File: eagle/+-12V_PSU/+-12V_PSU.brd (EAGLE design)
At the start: 93.7 x 71.1 mm, 23 parts, among them CN1 OUT, IC1 7812T, IC2 7912

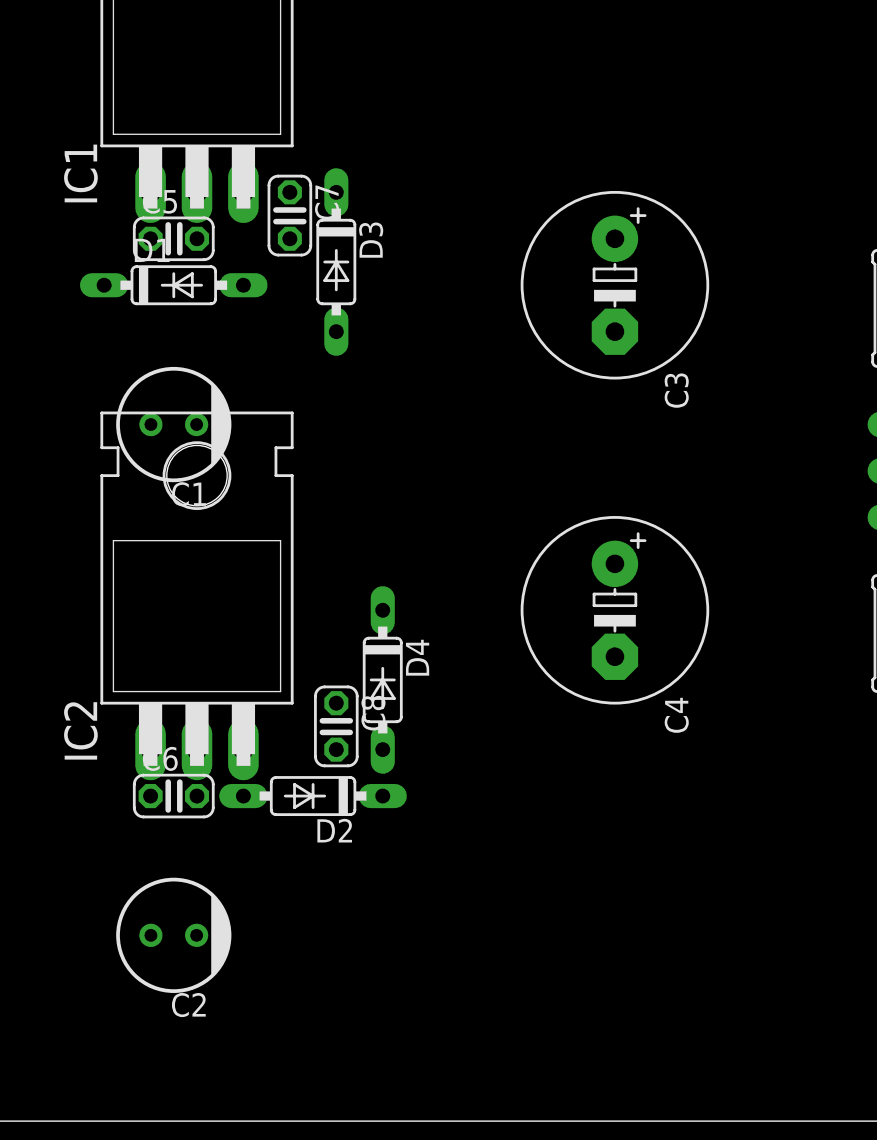
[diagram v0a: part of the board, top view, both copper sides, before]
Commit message: Add: +-12V_PSU eagle files
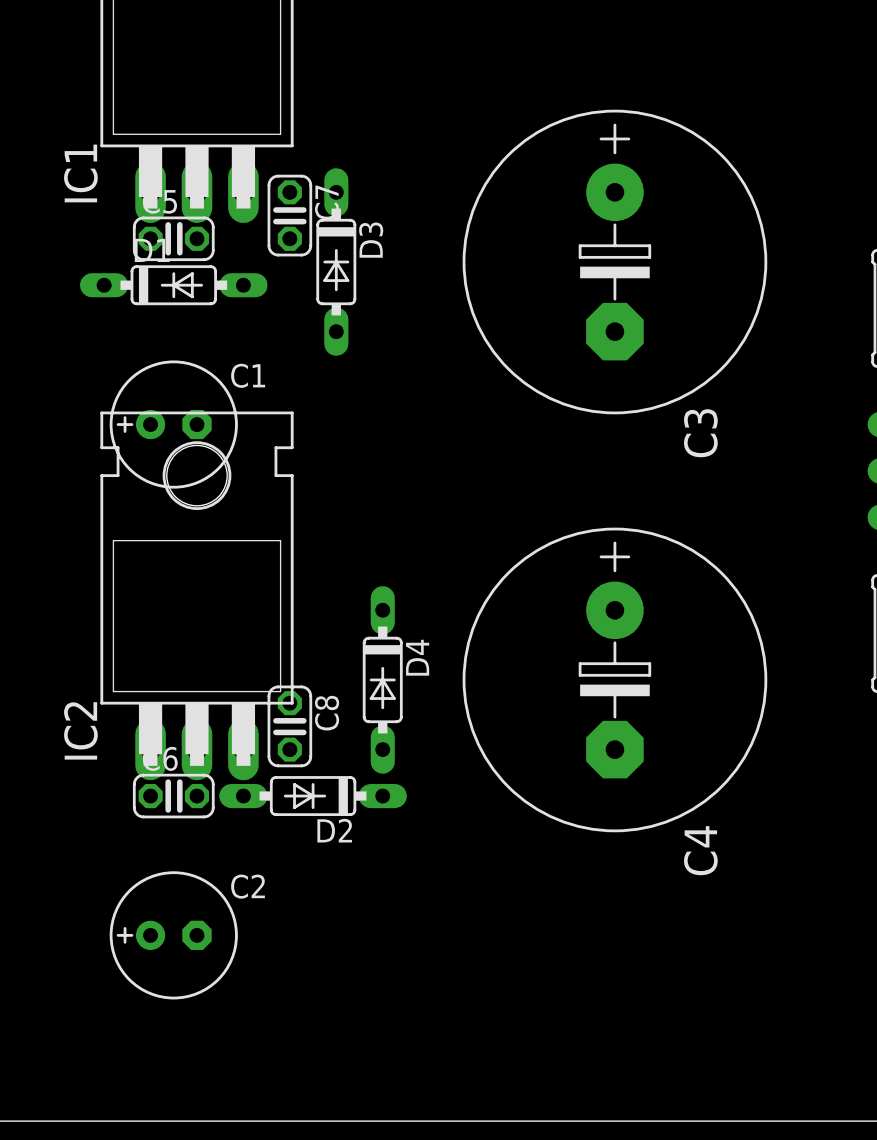
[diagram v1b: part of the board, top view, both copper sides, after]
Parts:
- C1, C2: device rcl:SANYO-OSCON_C6 -> rcl:E2,5-7
- C3, C4: device rcl:E5-10,5 -> rcl:E7,5-16
- moved C4 3.81 mm to (71.1, 24.1)
- moved C8 2.54 mm to (53.3, 21.6)
- moved C3 1.27 mm to (71.1, 47.0)
- turned C1 to 0 degrees
- turned C2 to 0 degrees
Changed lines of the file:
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@@
 <wire x1="2.54" y1="2.54" x2="2.54" y2="12.7" width="0" layer="100"/>
 <wire x1="2.54" y1="12.7" x2="2.54" y2="25.4" width="0" layer="100"/>
-<wire x1="2.54" y1="25.4" x2="2.54" y2="38.1" width="0" layer="100"/>
-<wire x1="2.54" y1="38.1" x2="2.54" y2="50.8" width="0" layer="100"/>
+<wire x1="2.54" y1="25.4" x2="5.08" y2="38.1" width="0" layer="100"/>
+<wire x1="5.08" y1="38.1" x2="2.54" y2="50.8" width="0" layer="100"/>
 <wire x1="2.54" y1="50.8" x2="2.54" y2="63.5" width="0" layer="100"/>
 <wire x1="2.54" y1="63.5" x2="2.54" y2="68.58" width="0" layer="100"/>
@@
 <wire x1="88.9" y1="2.54" x2="88.9" y2="68.58" width="0" layer="100"/>
 <wire x1="91.44" y1="2.54" x2="91.44" y2="12.7" width="0" layer="100"/>
-<wire x1="91.44" y1="12.7" x2="91.44" y2="38.1" width="0" layer="100"/>
-<wire x1="91.44" y1="38.1" x2="91.44" y2="50.8" width="0" layer="100"/>
+<wire x1="91.44" y1="12.7" x2="93.98" y2="38.1" width="0" layer="100"/>
+<wire x1="93.98" y1="38.1" x2="91.44" y2="50.8" width="0" layer="100"/>
 <wire x1="91.44" y1="50.8" x2="91.44" y2="68.58" width="0" layer="100"/>
 <wire x1="2.54" y1="12.7" x2="91.44" y2="12.7" width="0" layer="100"/>
 <wire x1="2.54" y1="25.4" x2="91.44" y2="25.4" width="0" layer="100"/>
-<wire x1="2.54" y1="38.1" x2="91.44" y2="38.1" width="0" layer="100"/>
+<wire x1="5.08" y1="38.1" x2="93.98" y2="38.1" width="0" layer="100"/>
 <wire x1="2.54" y1="63.5" x2="91.44" y2="63.5" width="0" layer="100"/>
 <wire x1="2.54" y1="68.58" x2="12.7" y2="68.58" width="0" layer="100"/>
@@
 </autorouter>
 <elements>
-<element name="C1" library="rcl" library_urn="urn:adsk.eagle:library:334" package="SANYO-OSCON_C6" package3d_urn="urn:adsk.eagle:package:23444/1" value="100uF" x="46.99" y="38.1" rot="R180">
-<attribute name="SPICEPREFIX" value="C" x="46.99" y="38.1" size="1.778" layer="27" rot="R180" display="off"/>
-</element>
-<element name="C2" library="rcl" library_urn="urn:adsk.eagle:library:334" package="SANYO-OSCON_C6" package3d_urn="urn:adsk.eagle:package:23444/1" value="100uF" x="46.99" y="10.16" rot="R180">
-<attribute name="SPICEPREFIX" value="C" x="46.99" y="10.16" size="1.778" layer="27" rot="R180" display="off"/>
-</element>
-<element name="C3" library="rcl" library_urn="urn:adsk.eagle:library:334" package="E5-10,5" package3d_urn="urn:adsk.eagle:package:23372/1" value="470uF" x="71.12" y="45.72" rot="R270">
-<attribute name="SPICEPREFIX" value="C" x="71.12" y="45.72" size="1.778" layer="27" rot="R270" display="off"/>
-</element>
-<element name="C4" library="rcl" library_urn="urn:adsk.eagle:library:334" package="E5-10,5" package3d_urn="urn:adsk.eagle:package:23372/1" value="470uF" x="71.12" y="27.94" rot="R270">
-<attribute name="SPICEPREFIX" value="C" x="71.12" y="27.94" size="1.778" layer="27" rot="R270" display="off"/>
+<element name="C1" library="rcl" library_urn="urn:adsk.eagle:library:334" package="E2,5-7" package3d_urn="urn:adsk.eagle:package:23345/1" value="100uF" x="46.99" y="38.1">
+<attribute name="SPICEPREFIX" value="C" x="46.99" y="38.1" size="1.778" layer="27" display="off"/>
+</element>
+<element name="C2" library="rcl" library_urn="urn:adsk.eagle:library:334" package="E2,5-7" package3d_urn="urn:adsk.eagle:package:23345/1" value="100uF" x="46.99" y="10.16">
+<attribute name="SPICEPREFIX" value="C" x="46.99" y="10.16" size="1.778" layer="27" display="off"/>
+</element>
+<element name="C3" library="rcl" library_urn="urn:adsk.eagle:library:334" package="E7,5-16" package3d_urn="urn:adsk.eagle:package:23382/2" value="470uF" x="71.12" y="46.99" rot="R270">
+<attribute name="SPICEPREFIX" value="C" x="71.12" y="46.99" size="1.778" layer="27" rot="R270" display="off"/>
+</element>
+<element name="C4" library="rcl" library_urn="urn:adsk.eagle:library:334" package="E7,5-16" package3d_urn="urn:adsk.eagle:package:23382/2" value="470uF" x="71.12" y="24.13" rot="R270">
+<attribute name="SPICEPREFIX" value="C" x="71.12" y="24.13" size="1.778" layer="27" rot="R270" display="off"/>
 </element>
 <element name="C5" library="rcl" library_urn="urn:adsk.eagle:library:334" package="C025-024X044" package3d_urn="urn:adsk.eagle:package:23630/1" value="0.33uF" x="46.99" y="48.26">
@@
 <attribute name="SPICEPREFIX" value="C" x="53.34" y="49.53" size="1.778" layer="27" rot="R270" display="off"/>
 </element>
-<element name="C8" library="rcl" library_urn="urn:adsk.eagle:library:334" package="C025-024X044" package3d_urn="urn:adsk.eagle:package:23630/1" value="0.1uF" x="55.88" y="21.59" rot="R270">
-<attribute name="SPICEPREFIX" value="C" x="55.88" y="21.59" size="1.778" layer="27" rot="R270" display="off"/>
+<element name="C8" library="rcl" library_urn="urn:adsk.eagle:library:334" package="C025-024X044" package3d_urn="urn:adsk.eagle:package:23630/1" value="0.1uF" x="53.34" y="21.59" rot="R270">
+<attribute name="SPICEPREFIX" value="C" x="53.34" y="21.59" size="1.778" layer="27" rot="R270" display="off"/>
 </element>
 <element name="CN1" library="mylib2" package="03PA" value="OUT" x="86.36" y="35.56" rot="R270"/>
@@
 <wire x1="90.17" y1="15.24" x2="91.44" y2="25.4" width="0" layer="19" extent="1-1"/>
 <wire x1="87.63" y1="15.24" x2="90.17" y2="15.24" width="0" layer="19" extent="1-1"/>
-<wire x1="71.12" y1="30.48" x2="86.36" y2="35.56" width="0" layer="19" extent="1-1"/>
-<wire x1="71.12" y1="43.18" x2="71.12" y2="30.48" width="0" layer="19" extent="1-1"/>
+<wire x1="71.12" y1="27.94" x2="86.36" y2="35.56" width="0" layer="19" extent="1-1"/>
+<wire x1="71.12" y1="43.18" x2="71.12" y2="27.94" width="0" layer="19" extent="1-1"/>
 <wire x1="55.88" y1="43.18" x2="71.12" y2="43.18" width="0" layer="19" extent="1-1"/>
 <wire x1="53.34" y1="48.26" x2="55.88" y2="43.18" width="0" layer="19" extent="1-1"/>
 <wire x1="48.26" y1="48.26" x2="53.34" y2="48.26" width="0" layer="19" extent="1-1"/>
 <wire x1="48.26" y1="50.8" x2="48.26" y2="48.26" width="0" layer="19" extent="1-1"/>
-<wire x1="48.24" y1="38.1" x2="48.26" y2="48.26" width="0" layer="19" extent="1-1"/>
-<wire x1="58.42" y1="27.94" x2="71.12" y2="30.48" width="0" layer="19" extent="1-1"/>
-<wire x1="55.88" y1="22.86" x2="58.42" y2="27.94" width="0" layer="19" extent="1-1"/>
-<wire x1="45.72" y1="20.32" x2="55.88" y2="22.86" width="0" layer="19" extent="1-1"/>
+<wire x1="48.26" y1="38.1" x2="48.26" y2="48.26" width="0" layer="19" extent="1-1"/>
+<wire x1="58.42" y1="27.94" x2="71.12" y2="27.94" width="0" layer="19" extent="1-1"/>
+<wire x1="53.34" y1="22.86" x2="58.42" y2="27.94" width="0" layer="19" extent="1-1"/>
+<wire x1="45.72" y1="20.32" x2="53.34" y2="22.86" width="0" layer="19" extent="1-1"/>
 <wire x1="45.72" y1="17.78" x2="45.72" y2="20.32" width="0" layer="19" extent="1-1"/>
-<wire x1="45.74" y1="10.16" x2="45.72" y2="17.78" width="0" layer="19" extent="1-1"/>
+<wire x1="45.72" y1="10.16" x2="45.72" y2="17.78" width="0" layer="19" extent="1-1"/>
 <wire x1="25.63" y1="27.86" x2="45.72" y2="20.32" width="0" layer="19" extent="1-1"/>
-<wire x1="25.63" y1="43.26" x2="48.24" y2="38.1" width="0" layer="19" extent="1-1"/>
+<wire x1="25.63" y1="43.26" x2="48.26" y2="38.1" width="0" layer="19" extent="1-1"/>
 </signal>
 <signal name="N$5">
@@
 <wire x1="48.26" y1="17.78" x2="48.26" y2="20.32" width="0" layer="19" extent="1-1"/>
 <wire x1="50.8" y1="17.78" x2="48.26" y2="17.78" width="0" layer="19" extent="1-1"/>
-<wire x1="48.24" y1="10.16" x2="48.26" y2="17.78" width="0" layer="19" extent="1-1"/>
+<wire x1="48.26" y1="10.16" x2="48.26" y2="17.78" width="0" layer="19" extent="1-1"/>
 <wire x1="25.63" y1="15.32" x2="48.26" y2="17.78" width="0" layer="19" extent="1-1"/>
 </signal>
@@
 <wire x1="45.72" y1="48.26" x2="45.72" y2="50.8" width="0" layer="19" extent="1-1"/>
 <wire x1="43.18" y1="45.72" x2="45.72" y2="48.26" width="0" layer="19" extent="1-1"/>
-<wire x1="45.74" y1="38.1" x2="43.18" y2="45.72" width="0" layer="19" extent="1-1"/>
+<wire x1="45.72" y1="38.1" x2="43.18" y2="45.72" width="0" layer="19" extent="1-1"/>
 <wire x1="25.63" y1="55.8" x2="45.72" y2="50.8" width="0" layer="19" extent="1-1"/>
 </signal>
@@
 <contactref element="CN1" pad="1"/>
 <wire x1="86.36" y1="38.1" x2="86.36" y2="40.64" width="0" layer="19" extent="1-1"/>
-<wire x1="71.12" y1="48.26" x2="86.36" y2="40.64" width="0" layer="19" extent="1-1"/>
-<wire x1="55.88" y1="50.8" x2="71.12" y2="48.26" width="0" layer="19" extent="1-1"/>
+<wire x1="71.12" y1="50.8" x2="86.36" y2="40.64" width="0" layer="19" extent="1-1"/>
+<wire x1="55.88" y1="50.8" x2="71.12" y2="50.8" width="0" layer="19" extent="1-1"/>
 <wire x1="53.34" y1="50.8" x2="55.88" y2="50.8" width="0" layer="19" extent="1-1"/>
 <wire x1="50.8" y1="50.8" x2="53.34" y2="50.8" width="0" layer="19" extent="1-1"/>
@@
 <contactref element="CN1" pad="3"/>
 <wire x1="86.36" y1="30.48" x2="86.36" y2="33.02" width="0" layer="19" extent="1-1"/>
-<wire x1="71.12" y1="25.4" x2="86.36" y2="33.02" width="0" layer="19" extent="1-1"/>
-<wire x1="58.42" y1="20.32" x2="71.12" y2="25.4" width="0" layer="19" extent="1-1"/>
+<wire x1="71.12" y1="20.32" x2="86.36" y2="33.02" width="0" layer="19" extent="1-1"/>
+<wire x1="58.42" y1="20.32" x2="71.12" y2="20.32" width="0" layer="19" extent="1-1"/>
 <wire x1="58.42" y1="17.78" x2="58.42" y2="20.32" width="0" layer="19" extent="1-1"/>
-<wire x1="55.88" y1="20.32" x2="58.42" y2="20.32" width="0" layer="19" extent="1-1"/>
-<wire x1="50.8" y1="20.32" x2="55.88" y2="20.32" width="0" layer="19" extent="1-1"/>
+<wire x1="53.34" y1="20.32" x2="58.42" y2="20.32" width="0" layer="19" extent="1-1"/>
+<wire x1="50.8" y1="20.32" x2="53.34" y2="20.32" width="0" layer="19" extent="1-1"/>
 </signal>
 <signal name="N$4">

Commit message: Update +-12V_PSU.brd
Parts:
- moved JP1 2.84 mm to (90.2, 12.7)
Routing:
- net GND: track 0.00 -> 222.5 mm
- net +12V: track 0.00 -> 48.4 mm
- net -12V: track 0.00 -> 45.9 mm
- net -15V: track 0.00 -> 45.1 mm
- net +15V: track 0.00 -> 37.5 mm
- net N$1: track 0.00 -> 23.3 mm
- net N$2: track 0.00 -> 20.7 mm
- net N$5: track 0.00 -> 20.7 mm
- net N$4: track 0.00 -> 5.08 mm
- net N$3: track 0.00 -> 5.08 mm

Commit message: +-12V_PSU Soldering Complete
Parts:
- turned LED2 to 270 degrees
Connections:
- net GND: now also LED2.A; no longer LED2.K
- net N$3: now also LED2.K; no longer LED2.A
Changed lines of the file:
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@@
 <element name="L2" library="mylib2" package="EV20" value="CM Choke" x="25.4" y="17.78" rot="R90"/>
 <element name="LED1" library="led" library_urn="urn:adsk.eagle:library:259" package="LED3MM" package3d_urn="urn:adsk.eagle:package:15797/1" value="RED" x="91.44" y="46.99" rot="R270"/>
-<element name="LED2" library="led" library_urn="urn:adsk.eagle:library:259" package="LED3MM" package3d_urn="urn:adsk.eagle:package:15797/1" value="Blue" x="91.44" y="24.13" rot="R90"/>
+<element name="LED2" library="led" library_urn="urn:adsk.eagle:library:259" package="LED3MM" package3d_urn="urn:adsk.eagle:package:15797/1" value="Blue" x="91.44" y="24.13" rot="R270"/>
 <element name="R1" library="rcl" library_urn="urn:adsk.eagle:library:334" package="0207/7" package3d_urn="urn:adsk.eagle:package:23493/1" value="1k" x="86.36" y="44.45" rot="R270">
 <attribute name="SPICEPREFIX" value="R" x="86.36" y="44.45" size="1.778" layer="27" rot="R270" display="off"/>
@@
 <contactref element="L1" pad="2"/>
 <contactref element="L2" pad="4"/>
-<contactref element="LED2" pad="K"/>
 <contactref element="CN1" pad="2"/>
 <wire x1="86.36" y1="35.56" x2="71.12" y2="35.56" width="1.016" layer="16"/>
@@
 <wire x1="71.12" y1="27.94" x2="71.12" y2="35.56" width="1.016" layer="16"/>
 <wire x1="91.44" y1="45.72" x2="91.44" y2="35.56" width="1.016" layer="16"/>
-<wire x1="91.44" y1="35.56" x2="91.44" y2="25.4" width="1.016" layer="16"/>
 <wire x1="86.36" y1="35.56" x2="91.44" y2="35.56" width="1.016" layer="16"/>
 <wire x1="48.26" y1="50.8" x2="48.26" y2="48.26" width="1.016" layer="16"/>
@@
 <wire x1="88.9" y1="12.7" x2="86.36" y2="12.7" width="1.016" layer="16"/>
 <wire x1="83.82" y1="15.24" x2="86.36" y2="12.7" width="1.016" layer="16"/>
-<wire x1="91.44" y1="25.4" x2="83.82" y2="25.4" width="1.016" layer="16"/>
-<wire x1="83.82" y1="25.4" x2="83.82" y2="15.24" width="1.016" layer="16"/>
+<wire x1="83.82" y1="15.24" x2="83.82" y2="25.4" width="1.016" layer="16"/>
+<contactref element="LED2" pad="A"/>
+<wire x1="83.82" y1="25.4" x2="91.44" y2="25.4" width="1.016" layer="16"/>
+<wire x1="91.44" y1="25.4" x2="91.44" y2="35.56" width="1.016" layer="16"/>
 </signal>
 <signal name="N$5">
@@
 <signal name="N$3">
 <contactref element="R2" pad="2"/>
-<contactref element="LED2" pad="A"/>
+<contactref element="LED2" pad="K"/>
 <wire x1="86.36" y1="22.86" x2="91.44" y2="22.86" width="0.4064" layer="16"/>
 </signal>
 </signals>
+<errors>
+</errors>
 </board>
 </drawing>
